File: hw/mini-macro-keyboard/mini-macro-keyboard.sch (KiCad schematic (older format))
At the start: 1 part

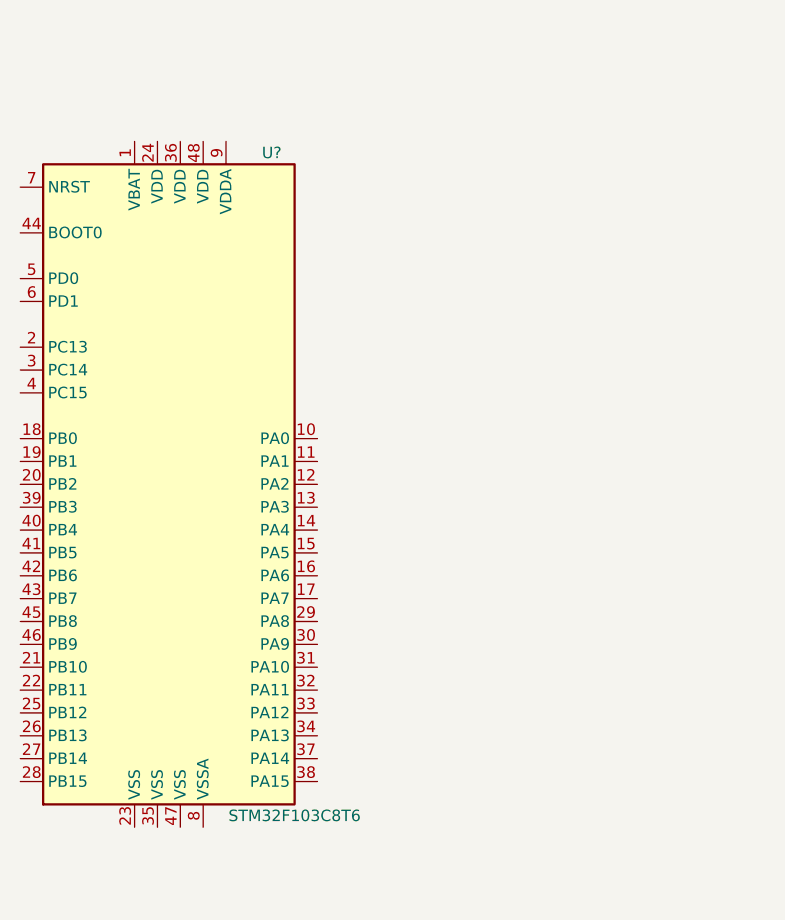
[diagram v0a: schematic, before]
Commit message: feat(hw): add power supply
Signed-off-by: Ivan Kovalenko <s1ckretbox@gmail.com>
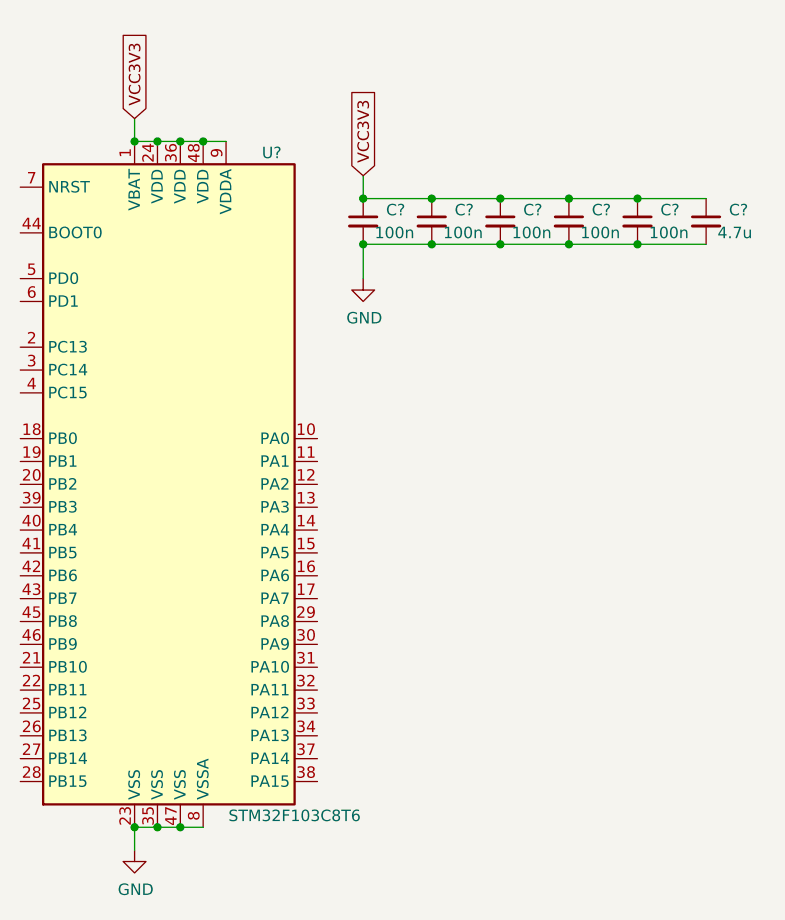
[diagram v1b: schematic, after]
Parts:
- added C? (x5): 100n, symbol Device:C_Small
- added C?: 4.7u, symbol Device:C_Small
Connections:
- net VCC3V3: now reaches U?.1 (VBAT)
- net VCC3V3: now also U?.24 (VDD), U?.36 (VDD), U?.48 (VDD), U?.9 (VDDA), C?.1, C?.1, C?.1, C?.1, C?.1, C?.1
- net GND: now reaches U?.23 (VSS)
- net GND: now also U?.35 (VSS), U?.47 (VSS), U?.8 (VSSA), C?.2, C?.2, C?.2, C?.2, C?.2, C?.2
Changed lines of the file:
@@
 	1    0    0    -1
 $EndComp
+$Comp
+L power:GND #PWR?
+U 1 1 5FF988F7
+P 2400 6450
+F 0 "#PWR?" H 2400 6200 50  0001 C CNN
+F 1 "GND" H 2405 6277 50  0000 C CNN
+F 2 "" H 2400 6450 50  0001 C CNN
+F 3 "" H 2400 6450 50  0001 C CNN
+	1    2400 6450
+	1    0    0    -1
+$EndComp
+Wire Wire Line
+	2400 6350 2400 6450
+Wire Wire Line
+	2400 6350 2500 6350
+Connection ~ 2400 6350
+Connection ~ 2500 6350
+Wire Wire Line
+	2500 6350 2600 6350
+Connection ~ 2600 6350
+Wire Wire Line
+	2600 6350 2700 6350
+Text GLabel 2400 3250 1    50   Input ~ 0
+VCC3V3
+Text GLabel 3400 3500 1    50   Input ~ 0
+VCC3V3
+Wire Wire Line
+	2400 3350 2500 3350
+Connection ~ 2500 3350
+Wire Wire Line
+	2500 3350 2600 3350
+Connection ~ 2600 3350
+Wire Wire Line
+	2600 3350 2700 3350
+Connection ~ 2700 3350
+Wire Wire Line
+	2700 3350 2800 3350
+Wire Wire Line
+	2400 3250 2400 3350
+Connection ~ 2400 3350
+$Comp
+L Device:C_Small C?
+U 1 1 5FF9BD70
+P 3400 3700
+F 0 "C?" H 3500 3750 50  0000 L CNN
+F 1 "100n" H 3450 3650 50  0000 L CNN
+F 2 "" H 3400 3700 50  0001 C CNN
+F 3 "~" H 3400 3700 50  0001 C CNN
+	1    3400 3700
+	1    0    0    -1
+$EndComp
+$Comp
+L Device:C_Small C?
+U 1 1 5FF9D075
+P 3700 3700
+F 0 "C?" H 3800 3750 50  0000 L CNN
+F 1 "100n" H 3750 3650 50  0000 L CNN
+F 2 "" H 3700 3700 50  0001 C CNN
+F 3 "~" H 3700 3700 50  0001 C CNN
+	1    3700 3700
+	1    0    0    -1
+$EndComp
+$Comp
+L Device:C_Small C?
+U 1 1 5FF9D4C1
+P 4000 3700
+F 0 "C?" H 4100 3750 50  0000 L CNN
+F 1 "100n" H 4050 3650 50  0000 L CNN
+F 2 "" H 4000 3700 50  0001 C CNN
+F 3 "~" H 4000 3700 50  0001 C CNN
+	1    4000 3700
+	1    0    0    -1
+$EndComp
+$Comp
+L Device:C_Small C?
+U 1 1 5FF9DB11
+P 4300 3700
+F 0 "C?" H 4400 3750 50  0000 L CNN
+F 1 "100n" H 4350 3650 50  0000 L CNN
+F 2 "" H 4300 3700 50  0001 C CNN
+F 3 "~" H 4300 3700 50  0001 C CNN
+	1    4300 3700
+	1    0    0    -1
+$EndComp
+$Comp
+L Device:C_Small C?
+U 1 1 5FF9DDD1
+P 4600 3700
+F 0 "C?" H 4700 3750 50  0000 L CNN
+F 1 "100n" H 4650 3650 50  0000 L CNN
+F 2 "" H 4600 3700 50  0001 C CNN
+F 3 "~" H 4600 3700 50  0001 C CNN
+	1    4600 3700
+	1    0    0    -1
+$EndComp
+$Comp
+L Device:C_Small C?
+U 1 1 5FF9E127
+P 4900 3700
+F 0 "C?" H 5000 3750 50  0000 L CNN
+F 1 "4.7u" H 4950 3650 50  0000 L CNN
+F 2 "" H 4900 3700 50  0001 C CNN
+F 3 "~" H 4900 3700 50  0001 C CNN
+	1    4900 3700
+	1    0    0    -1
+$EndComp
+Wire Wire Line
+	3400 3500 3400 3600
+Wire Wire Line
+	3400 3600 3700 3600
+Connection ~ 3400 3600
+Connection ~ 3700 3600
+Wire Wire Line
+	3700 3600 4000 3600
+Connection ~ 4000 3600
+Wire Wire Line
+	4000 3600 4300 3600
+Connection ~ 4300 3600
+Wire Wire Line
+	4300 3600 4600 3600
+Connection ~ 4600 3600
+Wire Wire Line
+	4600 3600 4900 3600
+Wire Wire Line
+	3400 3800 3700 3800
+Connection ~ 3700 3800
+Wire Wire Line
+	3700 3800 4000 3800
+Connection ~ 4000 3800
+Wire Wire Line
+	4000 3800 4300 3800
+Connection ~ 4300 3800
+Wire Wire Line
+	4300 3800 4600 3800
+Connection ~ 4600 3800
+Wire Wire Line
+	4600 3800 4900 3800
+$Comp
+L power:GND #PWR?
+U 1 1 5FF9F1E9
+P 3400 3950
+F 0 "#PWR?" H 3400 3700 50  0001 C CNN
+F 1 "GND" H 3405 3777 50  0000 C CNN
+F 2 "" H 3400 3950 50  0001 C CNN
+F 3 "" H 3400 3950 50  0001 C CNN
+	1    3400 3950
+	1    0    0    -1
+$EndComp
+Wire Wire Line
+	3400 3800 3400 3950
+Connection ~ 3400 3800
 $EndSCHEMATC

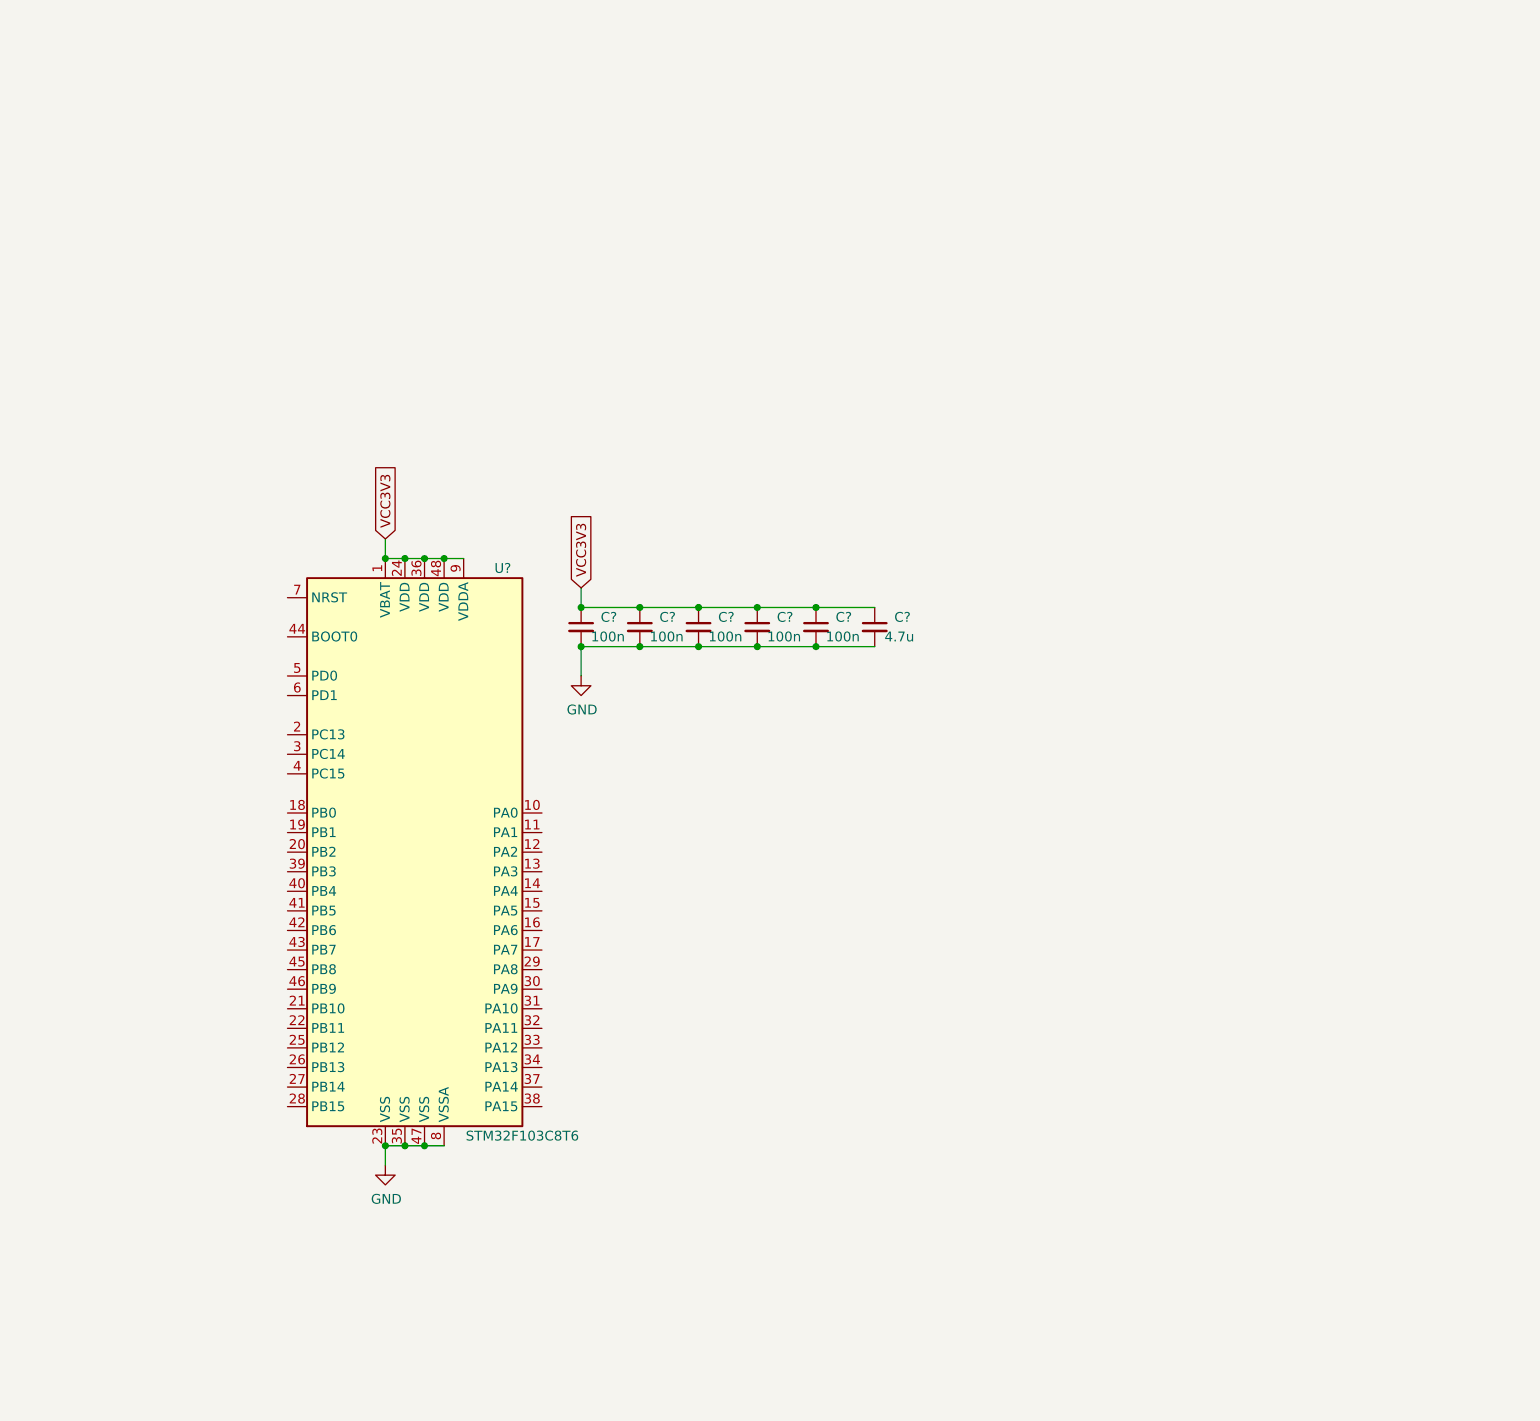
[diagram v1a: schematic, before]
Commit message: feat(hw): add boot0 switch
Signed-off-by: Ivan Kovalenko <s1ckretbox@gmail.com>
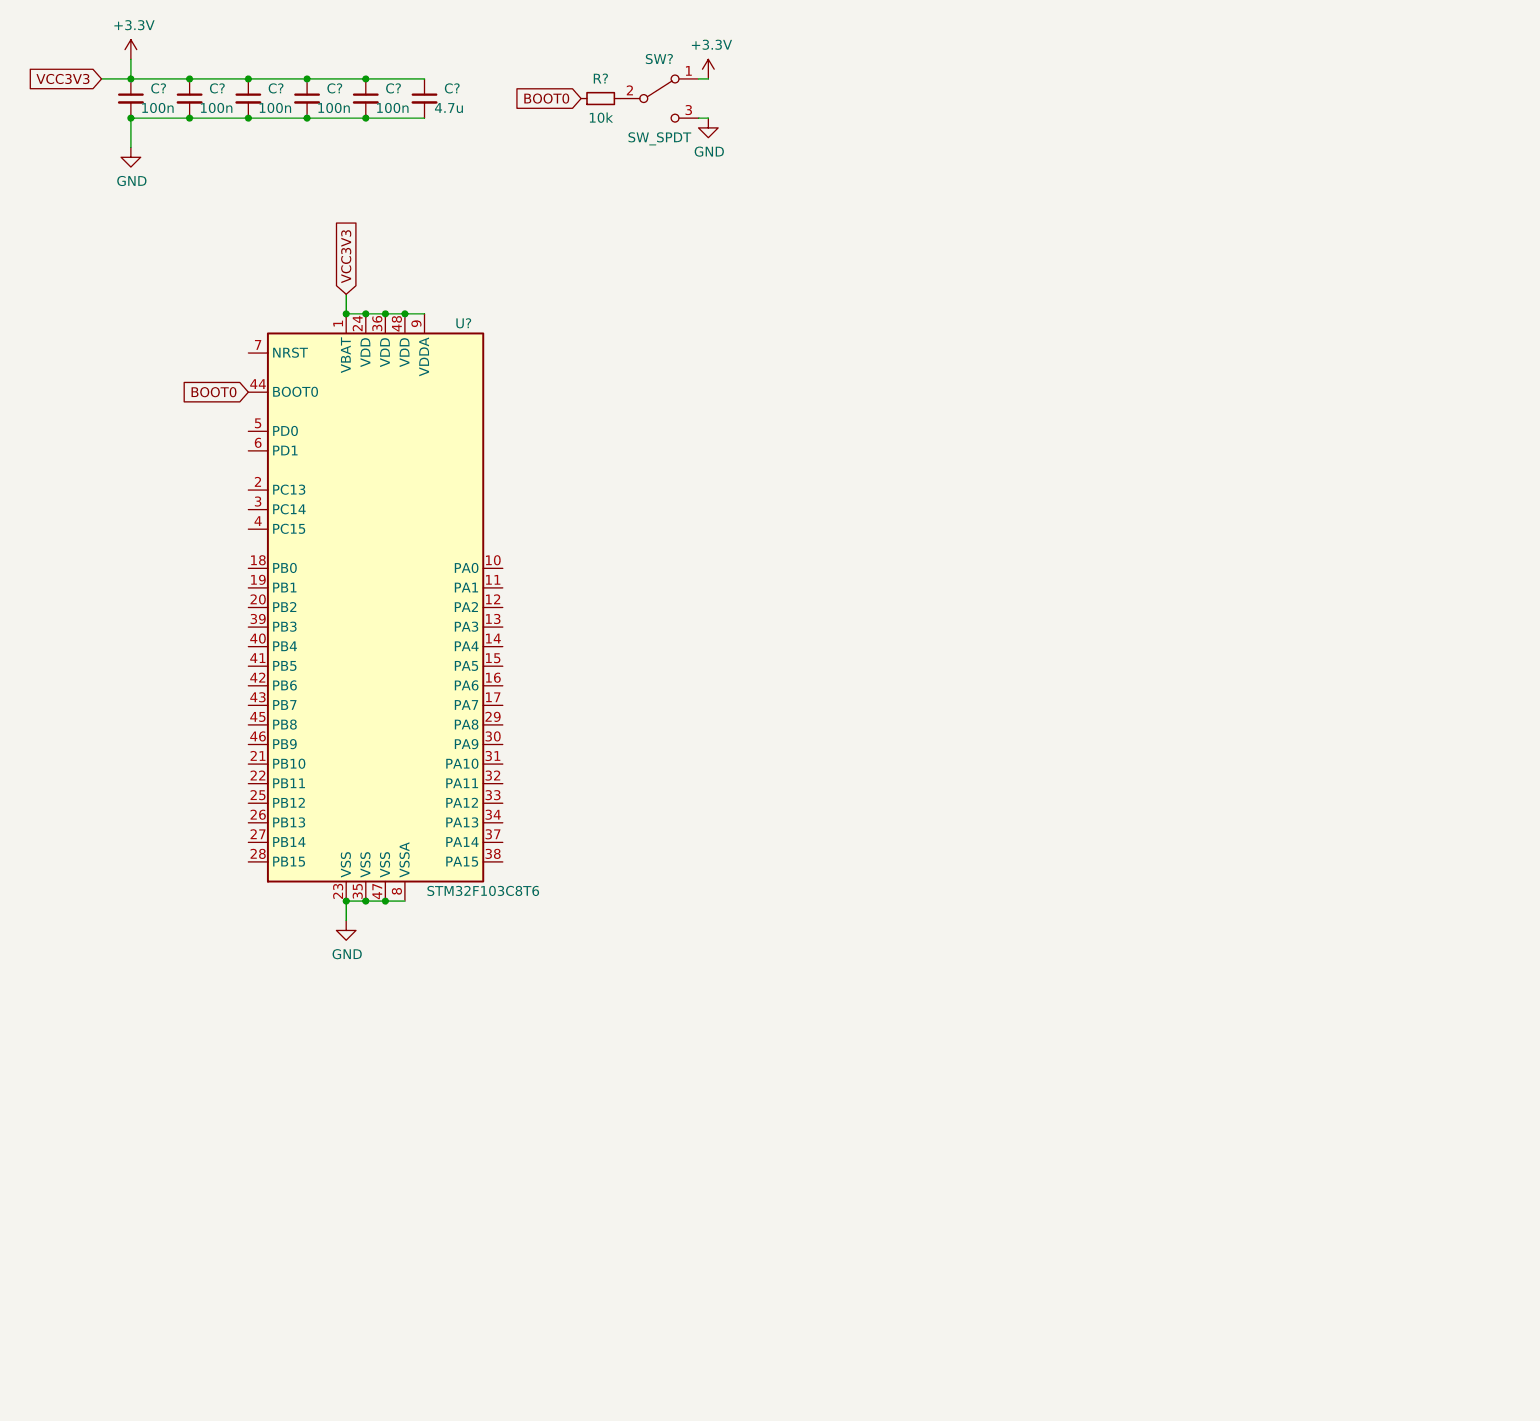
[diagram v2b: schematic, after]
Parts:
- added R?: 10k, symbol Device:R_Small
- added SW?: SW_SPDT, symbol Switch:SW_SPDT
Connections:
- net GND: now also SW?.3 (C)
- net BOOT0: now reaches U?.44 (BOOT0)
- net BOOT0: now also R?.1
- net VCC3V3 renamed +3V3
- net +3V3: now also SW?.1 (A)
- new net: R?.2, SW?.2 (B)
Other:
- moved on the sheet: C?, U?

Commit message: feat(hw): add nrst switch
Signed-off-by: Ivan Kovalenko <s1ckretbox@gmail.com>
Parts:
- added R?: 10k, symbol Device:R_Small
- added SW?: SW_SPST, symbol Switch:SW_SPST
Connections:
- net +3V3: now also R?.1; no longer C?.1
- net GND: now also SW?.1 (A)
- net NRST: now reaches U?.7 (NRST)
- net NRST: now also C?.1, R?.2, SW?.2 (B)
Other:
- moved on the sheet: C?, R?, SW?, U?

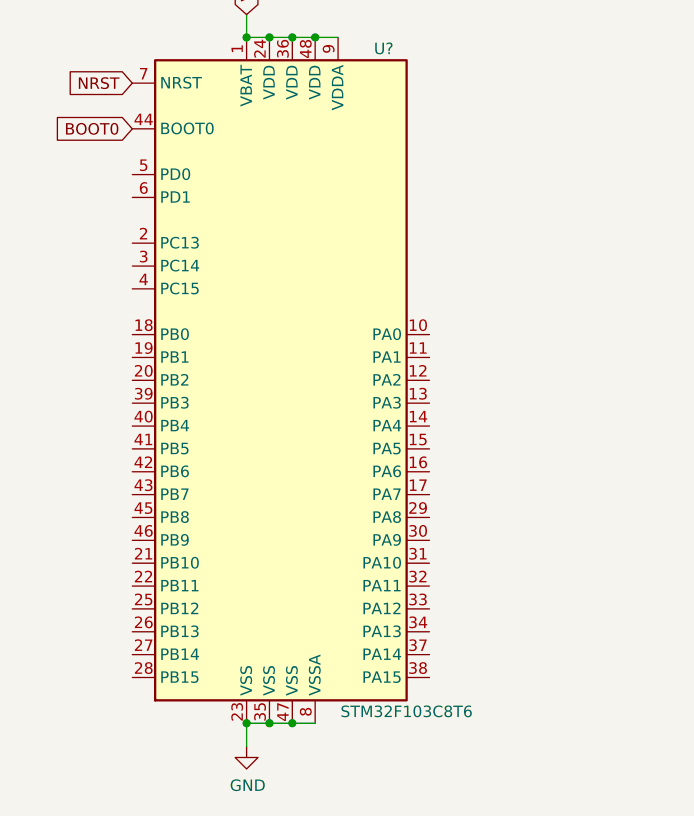
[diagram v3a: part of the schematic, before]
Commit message: feat(hw): add pin labels
Signed-off-by: Ivan Kovalenko <s1ckretbox@gmail.com>
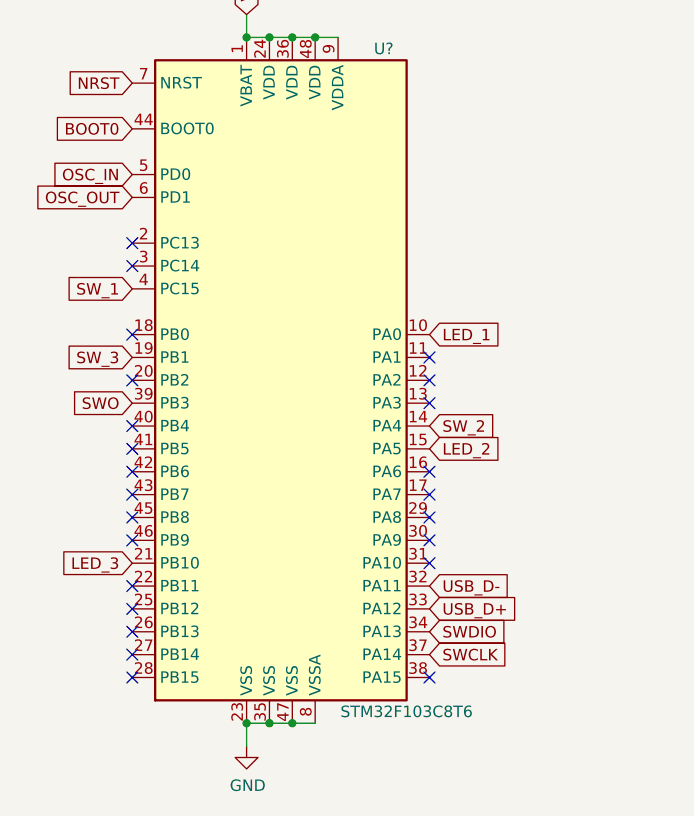
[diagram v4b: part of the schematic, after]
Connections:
- net LED_1: now reaches U?.10 (PA0)
- net SW_2: now reaches U?.14 (PA4)
- net LED_2: now reaches U?.15 (PA5)
- net SW_3: now reaches U?.19 (PB1)
- net LED_3: now reaches U?.21 (PB10)
- net USB_D-: now reaches U?.32 (PA11)
- net USB_D+: now reaches U?.33 (PA12)
- net SWDIO: now reaches U?.34 (PA13)
- net SWCLK: now reaches U?.37 (PA14)
- net SWO: now reaches U?.39 (PB3)
- net SW_1: now reaches U?.4 (PC15)
- net OSC_IN: now reaches U?.5 (PD0)
- net OSC_OUT: now reaches U?.6 (PD1)
- no-connect marks 0 -> 24
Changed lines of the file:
@@
 Wire Wire Line
 	3700 1500 3850 1500
+Text GLabel 1200 4950 0    50   Input ~ 0
+OSC_IN
+Text GLabel 1200 5050 0    50   Input ~ 0
+OSC_OUT
+Text GLabel 2500 6950 2    50   Input ~ 0
+SWDIO
+Text GLabel 2500 7050 2    50   Input ~ 0
+SWCLK
+Text GLabel 1200 5950 0    50   Input ~ 0
+SWO
+Text GLabel 2500 6850 2    50   Input ~ 0
+USB_D+
+Text GLabel 2500 6750 2    50   Input ~ 0
+USB_D-
+Text GLabel 1200 6650 0    50   Input ~ 0
+LED_3
+Text GLabel 2500 6150 2    50   Input ~ 0
+LED_2
+Text GLabel 2500 5650 2    50   Input ~ 0
+LED_1
+Text GLabel 1200 5450 0    50   Input ~ 0
+SW_1
+Text GLabel 2500 6050 2    50   Input ~ 0
+SW_2
+Text GLabel 1200 5750 0    50   Input ~ 0
+SW_3
+NoConn ~ 2500 5750
+NoConn ~ 2500 5850
+NoConn ~ 2500 5950
+NoConn ~ 2500 6250
+NoConn ~ 2500 6350
+NoConn ~ 2500 6450
+NoConn ~ 2500 6550
+NoConn ~ 2500 6650
+NoConn ~ 2500 7150
+NoConn ~ 1200 7150
+NoConn ~ 1200 7050
+NoConn ~ 1200 6950
+NoConn ~ 1200 6850
+NoConn ~ 1200 6750
+NoConn ~ 1200 6550
+NoConn ~ 1200 6450
+NoConn ~ 1200 6350
+NoConn ~ 1200 6250
+NoConn ~ 1200 6150
+NoConn ~ 1200 6050
+NoConn ~ 1200 5850
+NoConn ~ 1200 5650
+NoConn ~ 1200 5350
+NoConn ~ 1200 5250
 $EndSCHEMATC
